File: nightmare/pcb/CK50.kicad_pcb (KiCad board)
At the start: 2 copper layers, 305 x 95 mm, 107 parts, among them K0 KEYSW, K1 KEYSW, K10 KEYSW, K11 KEYSW, K12 KEYSW, K13 KEYSW, K14 KEYSW, K15 KEYSW, K16 KEYSW, K17 KEYSW, K18 KEYSW, K19 KEYSW, K2 KEYSW, K20 KEYSW, K21 KEYSW, K22 KEYSW, K23 KEYSW, K24 KEYSW, K25 KEYSW, K26 KEYSW, K27 KEYSW, K28 KEYSW, K29 KEYSW, K3 KEYSW, K30 KEYSW, K31 KEYSW, K32 KEYSW, K33 KEYSW, K34 KEYSW, K35 KEYSW, K36 KEYSW, K37 KEYSW, K38 KEYSW, K39 KEYSW, K4 KEYSW, K40 KEYSW, K41 KEYSW, K420 KEYSW, K43 KEYSW, K44 KEYSW, K45 KEYSW, K46 KEYSW, K47 KEYSW, K48 KEYSW, K5 KEYSW, K6 KEYSW, K7 KEYSW, K8 KEYSW, K9 KEYSW, U0 ProMicro

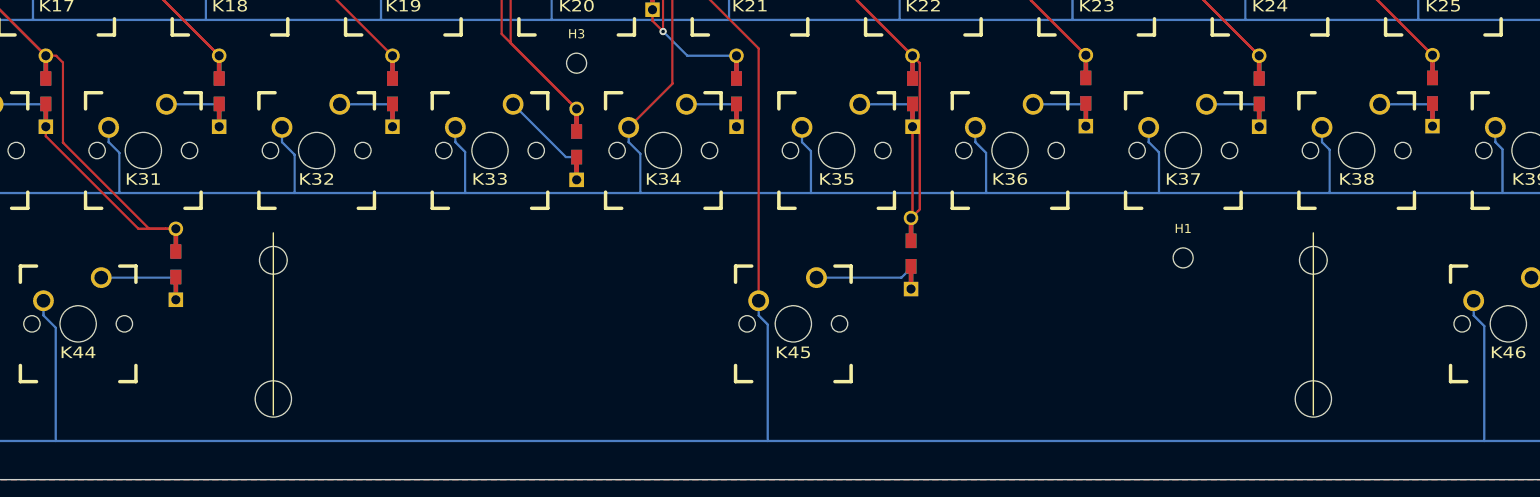
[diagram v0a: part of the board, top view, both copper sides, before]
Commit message: updated PCB for split space
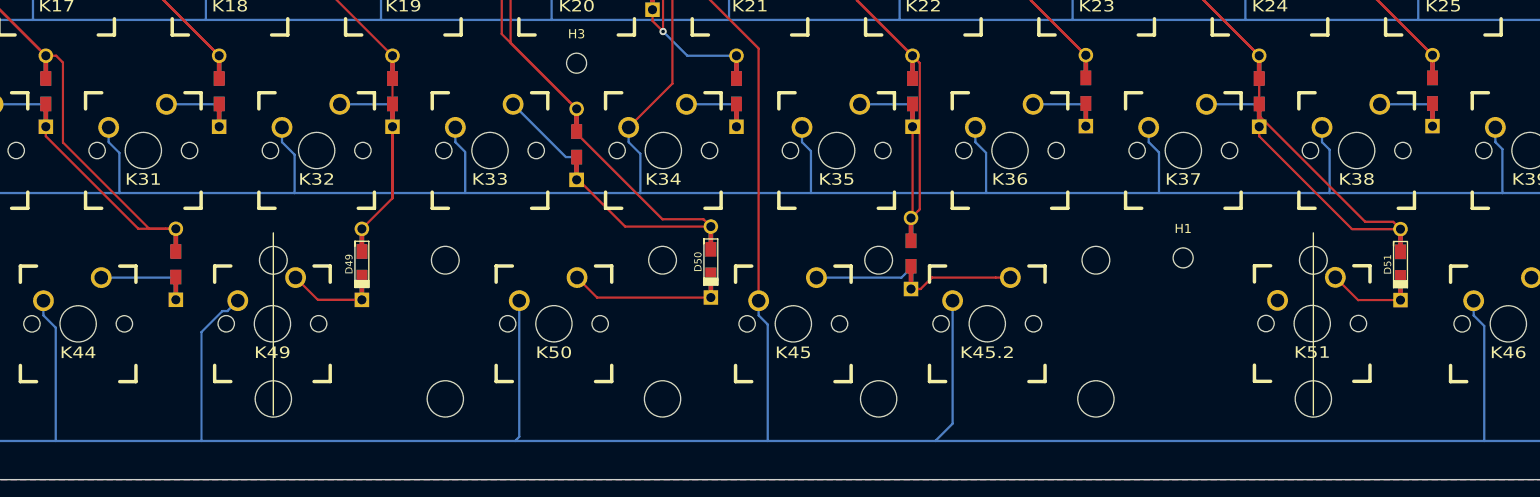
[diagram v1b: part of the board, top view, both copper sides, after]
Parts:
- added D49: 1N4148, Keebio-Parts:Diode-dual, F.Cu at (287.1, 161.3)
- added D50: 1N4148, Keebio-Parts:Diode-dual, F.Cu at (325.5, 161.1)
- added D51: 1N4148, Keebio-Parts:Diode-dual, F.Cu at (401.3, 161.4)
- added K45.2: KEYSW, Keebio-Parts:MX_PCB_275H, F.Cu at (355.9, 167.9)
- added K49: KEYSW, Keebio-Parts:MX_PCB_100H, F.Cu at (277.3, 167.9)
- added K50: KEYSW, Keebio-Parts:MX_PCB_225H, F.Cu at (308.3, 167.9)
- added K51: KEYSW, Keebio-Parts:MX_PCB_100H, F.Cu at (391.6, 167.8)
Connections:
- D32 pad 1: Net-(D32-Pad1) -> /col4
- D33 pad 1: Net-(D33-Pad1) -> /col5
- D37 pad 1: Net-(D37-Pad1) -> /col9
- K32 pad 1: Net-(D32-Pad1) -> /col4
- K33 pad 1: Net-(D33-Pad1) -> /col5
- K37 pad 1: Net-(D37-Pad1) -> /col9
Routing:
- net /col9: track 133.7 -> 187.6 mm
- net /row3: track 413.7 -> 462.9 mm
- net /col5: track 112.9 -> 161.9 mm
- net /col4: track 108.9 -> 141.8 mm
- net Net-(D50-Pad1): track 0.00 -> 15.6 mm
- net Net-(D45-Pad1): track 11.0 -> 22.5 mm
- net Net-(D33-Pad1): track 9.39 -> 0.00 mm
- net Net-(D49-Pad1): track 0.00 -> 8.31 mm
- net Net-(D51-Pad1): track 0.00 -> 8.20 mm
- net Net-(D37-Pad1): track 5.81 -> 0.00 mm
- net Net-(D32-Pad1): track 5.81 -> 0.00 mm

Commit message: updated PCB for revC and added split space plate
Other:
- board text added: "Crossed Keys Nightmare revC"
- board text removed: "Crossed Keys Nightmare revB"

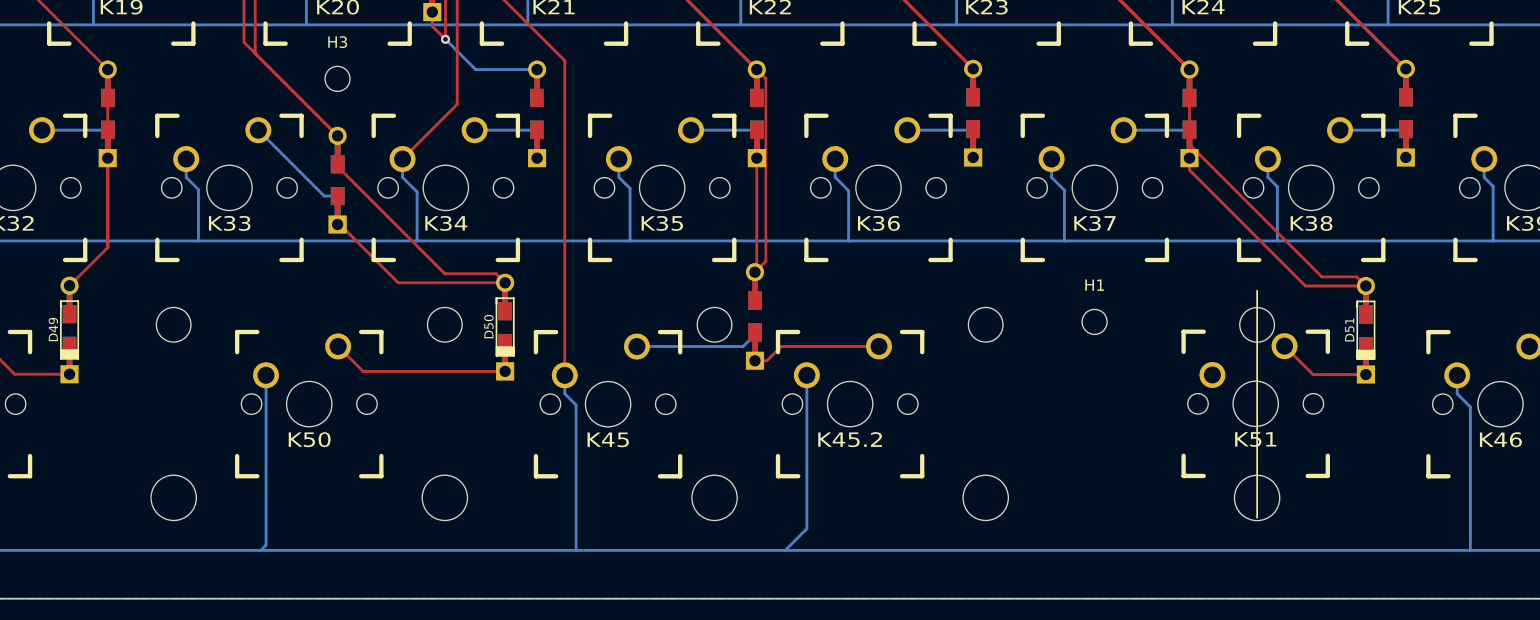
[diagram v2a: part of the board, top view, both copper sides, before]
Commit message: fixed missing wire
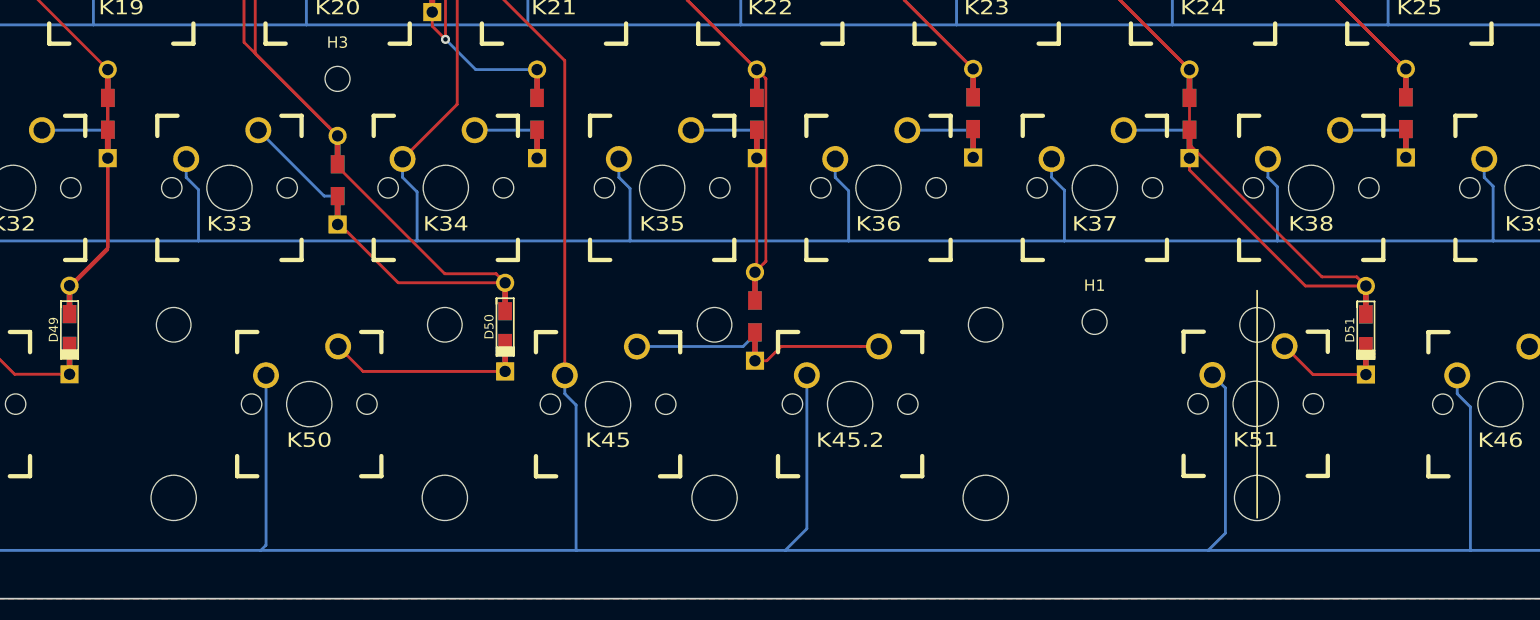
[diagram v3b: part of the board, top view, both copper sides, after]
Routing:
- net /col4: track 141.8 -> 163.4 mm
- net /row3: track 462.9 -> 479.4 mm
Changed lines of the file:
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@@
     (thickness 1.6)
     (drawings 2324)
-    (tracks 748)
+    (tracks 756)
     (zones 0)
     (modules 114)
@@
   (segment (start 280.987264 128.885048) (end 283.9974 131.895184) (width 0.25) (layer F.Cu) (net 5))
   (segment (start 283.9974 131.895184) (end 290.512256 138.41004) (width 0.25) (layer F.Cu) (net 5))
+  (segment (start 290.474296 143.748) (end 290.512256 143.71004) (width 0.25) (layer B.Cu) (net 5))
+  (segment (start 284.717888 143.748) (end 290.474296 143.748) (width 0.25) (layer B.Cu) (net 5))
+  (segment (start 290.512256 146.21004) (end 290.512256 154.075544) (width 0.25) (layer F.Cu) (net 5))
+  (segment (start 290.512256 154.075544) (end 290.512256 139.61004) (width 0.25) (layer F.Cu) (net 5))
+  (segment (start 287.147 157.4408) (end 290.512256 154.075544) (width 0.25) (layer F.Cu) (net 5))
+  (segment (start 290.512256 139.54141) (end 290.512256 138.41004) (width 0.25) (layer F.Cu) (net 5))
+  (segment (start 290.512256 154.275544) (end 290.512256 139.54141) (width 0.25) (layer F.Cu) (net 5))
+  (segment (start 287.147 157.6408) (end 290.512256 154.275544) (width 0.25) (layer F.Cu) (net 5))
+  (segment (start 287.147 158.6408) (end 287.147 157.6408) (width 0.25) (layer F.Cu) (net 5))
   (segment (start 316.522101 105.072181) (end 317.3984 105.94848) (width 0.25) (layer B.Cu) (net 6))
   (segment (start 315.629951 104.180031) (end 316.522101 105.072181) (width 0.25) (layer B.Cu) (net 6))
@@
   (segment (start 302.514 136.014) (end 309.950001 143.450001) (width 0.25) (layer F.Cu) (net 6))
   (segment (start 302.514 120.644494) (end 302.514 136.014) (width 0.25) (layer F.Cu) (net 6))
+  (segment (start 309.569872 149.55) (end 310.75 149.55) (width 0.25) (layer B.Cu) (net 6))
+  (segment (start 303.767872 143.748) (end 309.569872 149.55) (width 0.25) (layer B.Cu) (net 6))
+  (segment (start 310.75 151.85) (end 310.75 150.85) (width 0.25) (layer F.Cu) (net 6))
+  (segment (start 316.0868 157.1868) (end 310.75 151.85) (width 0.25) (layer F.Cu) (net 6))
+  (segment (start 325.501 157.1868) (end 316.0868 157.1868) (width 0.25) (layer F.Cu) (net 6))
+  (segment (start 310.75 145.38137) (end 310.75 144.25) (width 0.25) (layer F.Cu) (net 6))
+  (segment (start 310.75 146.95) (end 310.75 145.38137) (width 0.25) (layer F.Cu) (net 6))
+  (segment (start 320.186801 156.386801) (end 310.75 146.95) (width 0.25) (layer F.Cu) (net 6))
+  (segment (start 324.701001 156.386801) (end 320.186801 156.386801) (width 0.25) (layer F.Cu) (net 6))
+  (segment (start 325.501 157.1868) (end 324.701001 156.386801) (width 0.25) (layer F.Cu) (net 6))
   (segment (start 314.324736 120.787392) (end 319.087232 125.549888) (width 0.25) (layer F.Cu) (net 7))
   (segment (start 314.324736 113.735064) (end 314.324736 120.787392) (width 0.25) (layer F.Cu) (net 7))
@@
   (segment (start 372.622747 115.684675) (end 376.237184 119.299112) (width 0.25) (layer F.Cu) (net 10))
   (segment (start 372.622747 107.002247) (end 372.622747 115.684675) (width 0.25) (layer F.Cu) (net 10))
+  (segment (start 385.724216 143.748) (end 385.762176 143.71004) (width 0.25) (layer B.Cu) (net 10))
+  (segment (start 379.967808 143.748) (end 385.724216 143.748) (width 0.25) (layer B.Cu) (net 10))
+  (segment (start 385.762176 147.26004) (end 385.762176 146.21004) (width 0.25) (layer F.Cu) (net 10))
+  (segment (start 395.968336 157.4662) (end 385.762176 147.26004) (width 0.25) (layer F.Cu) (net 10))
+  (segment (start 401.2946 157.4662) (end 395.968336 157.4662) (width 0.25) (layer F.Cu) (net 10))
+  (segment (start 385.762176 139.54141) (end 385.762176 138.41004) (width 0.25) (layer F.Cu) (net 10))
+  (segment (start 385.762176 145.005386) (end 385.762176 139.54141) (width 0.25) (layer F.Cu) (net 10))
+  (segment (start 397.422991 156.666201) (end 385.762176 145.005386) (width 0.25) (layer F.Cu) (net 10))
+  (segment (start 400.494601 156.666201) (end 397.422991 156.666201) (width 0.25) (layer F.Cu) (net 10))
+  (segment (start 401.2946 157.4662) (end 400.494601 156.666201) (width 0.25) (layer F.Cu) (net 10))
   (segment (start 390.347808 111.265536) (end 390.524672 111.265536) (width 0.25) (layer B.Cu) (net 11))
   (segment (start 384.730304 105.648032) (end 390.347808 111.265536) (width 0.25) (layer B.Cu) (net 11))
@@
   (segment (start 271.424312 143.748) (end 271.462272 143.71004) (width 0.25) (layer B.Cu) (net 15))
   (segment (start 265.667904 143.748) (end 271.424312 143.748) (width 0.25) (layer B.Cu) (net 15))
-  (segment (start 290.474296 143.748) (end 290.512256 143.71004) (width 0.25) (layer B.Cu) (net 5))
-  (segment (start 284.717888 143.748) (end 290.474296 143.748) (width 0.25) (layer B.Cu) (net 5))
-  (segment (start 290.512256 146.21004) (end 290.512256 154.075544) (width 0.25) (layer F.Cu) (net 5))
-  (segment (start 290.512256 154.075544) (end 290.512256 139.61004) (width 0.25) (layer F.Cu) (net 5))
-  (segment (start 287.147 157.4408) (end 290.512256 154.075544) (width 0.25) (layer F.Cu) (net 5))
-  (segment (start 309.569872 149.55) (end 310.75 149.55) (width 0.25) (layer B.Cu) (net 6))
-  (segment (start 303.767872 143.748) (end 309.569872 149.55) (width 0.25) (layer B.Cu) (net 6))
-  (segment (start 310.75 151.85) (end 310.75 150.85) (width 0.25) (layer F.Cu) (net 6))
-  (segment (start 316.0868 157.1868) (end 310.75 151.85) (width 0.25) (layer F.Cu) (net 6))
-  (segment (start 325.501 157.1868) (end 316.0868 157.1868) (width 0.25) (layer F.Cu) (net 6))
-  (segment (start 310.75 145.38137) (end 310.75 144.25) (width 0.25) (layer F.Cu) (net 6))
-  (segment (start 310.75 146.95) (end 310.75 145.38137) (width 0.25) (layer F.Cu) (net 6))
-  (segment (start 320.186801 156.386801) (end 310.75 146.95) (width 0.25) (layer F.Cu) (net 6))
-  (segment (start 324.701001 156.386801) (end 320.186801 156.386801) (width 0.25) (layer F.Cu) (net 6))
-  (segment (start 325.501 157.1868) (end 324.701001 156.386801) (width 0.25) (layer F.Cu) (net 6))
   (segment (start 328.276608 143.748) (end 328.314568 143.71004) (width 0.25) (layer B.Cu) (net 16))
   (segment (start 322.817856 143.748) (end 328.276608 143.748) (width 0.25) (layer B.Cu) (net 16))
   (segment (start 366.613288 143.748) (end 366.712192 143.649096) (width 0.25) (layer B.Cu) (net 17))
   (segment (start 360.917824 143.748) (end 366.613288 143.748) (width 0.25) (layer B.Cu) (net 17))
-  (segment (start 385.724216 143.748) (end 385.762176 143.71004) (width 0.25) (layer B.Cu) (net 10))
-  (segment (start 379.967808 143.748) (end 385.724216 143.748) (width 0.25) (layer B.Cu) (net 10))
-  (segment (start 385.762176 147.26004) (end 385.762176 146.21004) (width 0.25) (layer F.Cu) (net 10))
-  (segment (start 395.968336 157.4662) (end 385.762176 147.26004) (width 0.25) (layer F.Cu) (net 10))
-  (segment (start 401.2946 157.4662) (end 395.968336 157.4662) (width 0.25) (layer F.Cu) (net 10))
-  (segment (start 385.762176 139.54141) (end 385.762176 138.41004) (width 0.25) (layer F.Cu) (net 10))
-  (segment (start 385.762176 145.005386) (end 385.762176 139.54141) (width 0.25) (layer F.Cu) (net 10))
-  (segment (start 397.422991 156.666201) (end 385.762176 145.005386) (width 0.25) (layer F.Cu) (net 10))
-  (segment (start 400.494601 156.666201) (end 397.422991 156.666201) (width 0.25) (layer F.Cu) (net 10))
-  (segment (start 401.2946 157.4662) (end 400.494601 156.666201) (width 0.25) (layer F.Cu) (net 10))
   (segment (start 404.713256 143.748) (end 404.81216 143.649096) (width 0.25) (layer B.Cu) (net 18))
   (segment (start 399.017792 143.748) (end 404.713256 143.748) (width 0.25) (layer B.Cu) (net 18))
@@
   (segment (start 352.0694 165.3286) (end 352.0694 178.845) (width 0.25) (layer B.Cu) (net 29))
   (segment (start 331.75 180.75) (end 350.1644 180.75) (width 0.25) (layer B.Cu) (net 29))
-  (segment (start 350.1644 180.75) (end 410.5 180.75) (width 0.25) (layer B.Cu) (net 29))
+  (segment (start 388.924799 179.226001) (end 387.4008 180.75) (width 0.25) (layer B.Cu) (net 29))
+  (segment (start 388.924799 166.446199) (end 388.924799 179.226001) (width 0.25) (layer B.Cu) (net 29))
+  (segment (start 387.7818 165.3032) (end 388.924799 166.446199) (width 0.25) (layer B.Cu) (net 29))
+  (segment (start 350.1644 180.75) (end 387.4008 180.75) (width 0.25) (layer B.Cu) (net 29))
+  (segment (start 387.4008 180.75) (end 410.5 180.75) (width 0.25) (layer B.Cu) (net 29))
   (segment (start 282.3094 165.2408) (end 279.8572 162.7886) (width 0.25) (layer F.Cu) (net 34))
   (segment (start 287.147 165.2408) (end 282.3094 165.2408) (width 0.25) (layer F.Cu) (net 34))

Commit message: Update Nightmare PCB to fix NKRO
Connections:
- net VCC renamed Net-(U0-Pad21)
- D0 pad 1: /col0 -> Net-(D0-Pad1)
- D1 pad 1: /col1 -> Net-(D1-Pad1)
- D11 pad 1: /col11 -> Net-(D11-Pad1)
- D12 pad 1: /col12 -> Net-(D12-Pad1)
- D13 pad 1: /col13 -> Net-(D13-Pad1)
- D14 pad 1: /col0 -> Net-(D14-Pad1)
- D15 pad 1: /col1 -> Net-(D15-Pad1)
- D16 pad 1: /col2 -> Net-(D16-Pad1)
- D17 pad 1: /col3 -> Net-(D17-Pad1)
- D18 pad 1: /col4 -> Net-(D18-Pad1)
- D19 pad 1: /col5 -> Net-(D19-Pad1)
- D2 pad 1: /col2 -> Net-(D2-Pad1)
- D20 pad 1: /col6 -> Net-(D20-Pad1)
- D21 pad 1: /col7 -> Net-(D21-Pad1)
- D22 pad 1: /col8 -> Net-(D22-Pad1)
- D23 pad 1: /col9 -> Net-(D23-Pad1)
- D24 pad 1: /col10 -> Net-(D24-Pad1)
- D25 pad 1: /col11 -> Net-(D25-Pad1)
- D26 pad 1: /col12 -> Net-(D26-Pad1)
- D27 pad 1: /col13 -> Net-(D27-Pad1)
- D28 pad 1: /col0 -> Net-(D28-Pad1)
- D29 pad 1: /col1 -> Net-(D29-Pad1)
- D3 pad 1: /col3 -> Net-(D3-Pad1)
- D30 pad 1: /col2 -> Net-(D30-Pad1)
- D32 pad 1: /col4 -> Net-(D32-Pad1)
- D33 pad 1: /col5 -> Net-(D33-Pad1)
- D35 pad 1: /col7 -> Net-(D35-Pad1)
- D37 pad 1: /col9 -> Net-(D37-Pad1)
- D39 pad 1: /col11 -> Net-(D39-Pad1)
- D4 pad 1: /col4 -> Net-(D4-Pad1)
- D40 pad 1: /col12 -> Net-(D40-Pad1)
- D41 pad 1: /col13 -> Net-(D41-Pad1)
- D5 pad 1: /col5 -> Net-(D5-Pad1)
- D6 pad 1: /col6 -> Net-(D6-Pad1)
- D7 pad 1: /col7 -> Net-(D7-Pad1)
- D8 pad 1: /col8 -> Net-(D8-Pad1)
- D9 pad 1: /col9 -> Net-(D9-Pad1)
- K0 pad 1: /col0 -> Net-(D0-Pad1)
- K1 pad 1: /col1 -> Net-(D1-Pad1)
- K11 pad 1: /col11 -> Net-(D11-Pad1)
- K12 pad 1: /col12 -> Net-(D12-Pad1)
- K13 pad 1: /col13 -> Net-(D13-Pad1)
- K14 pad 1: /col0 -> Net-(D14-Pad1)
- K15 pad 1: /col1 -> Net-(D15-Pad1)
- K16 pad 1: /col2 -> Net-(D16-Pad1)
- K17 pad 1: /col3 -> Net-(D17-Pad1)
- K18 pad 1: /col4 -> Net-(D18-Pad1)
- K19 pad 1: /col5 -> Net-(D19-Pad1)
- K2 pad 1: /col2 -> Net-(D2-Pad1)
- K20 pad 1: /col6 -> Net-(D20-Pad1)
- K21 pad 1: /col7 -> Net-(D21-Pad1)
- K22 pad 1: /col8 -> Net-(D22-Pad1)
- K23 pad 1: /col9 -> Net-(D23-Pad1)
- K24 pad 1: /col10 -> Net-(D24-Pad1)
- K25 pad 1: /col11 -> Net-(D25-Pad1)
- K26 pad 1: /col12 -> Net-(D26-Pad1)
- K27 pad 1: /col13 -> Net-(D27-Pad1)
- K28 pad 1: /col0 -> Net-(D28-Pad1)
- K29 pad 1: /col1 -> Net-(D29-Pad1)
- K3 pad 1: /col3 -> Net-(D3-Pad1)
- K30 pad 1: /col2 -> Net-(D30-Pad1)
- K32 pad 1: /col4 -> Net-(D32-Pad1)
- K33 pad 1: /col5 -> Net-(D33-Pad1)
- K35 pad 1: /col7 -> Net-(D35-Pad1)
- K37 pad 1: /col9 -> Net-(D37-Pad1)
- K39 pad 1: /col11 -> Net-(D39-Pad1)
- K4 pad 1: /col4 -> Net-(D4-Pad1)
- K40 pad 1: /col12 -> Net-(D40-Pad1)
- K41 pad 1: /col13 -> Net-(D41-Pad1)
- K5 pad 1: /col5 -> Net-(D5-Pad1)
- K6 pad 1: /col6 -> Net-(D6-Pad1)
- K7 pad 1: /col7 -> Net-(D7-Pad1)
- K8 pad 1: /col8 -> Net-(D8-Pad1)
- K9 pad 1: /col9 -> Net-(D9-Pad1)
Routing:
- net /col1: track 264.0 -> 189.7 mm
- net /col4: track 163.4 -> 101.5 mm
- net /col2: track 215.1 -> 154.2 mm
- net /col5: track 161.9 -> 101.8 mm
- net /col9: track 187.6 -> 129.4 mm
- net /col13: track 348.3 -> 292.6 mm
- net /col7: track 113.2 -> 58.6 mm
- net /col11: track 225.3 -> 171.8 mm
- net /col0: track 251.0 -> 203.3 mm
- net /col8: track 108.2 -> 71.3 mm
- net /col3: track 140.4 -> 103.7 mm
- net /col10: track 161.8 -> 133.4 mm
- net /col6: track 95.8 -> 69.2 mm
- net /col12: track 236.0 -> 213.5 mm
- net Net-(D29-Pad1): track 0.00 -> 15.1 mm
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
